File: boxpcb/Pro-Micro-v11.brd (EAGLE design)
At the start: 40 x 74 mm, 30 parts

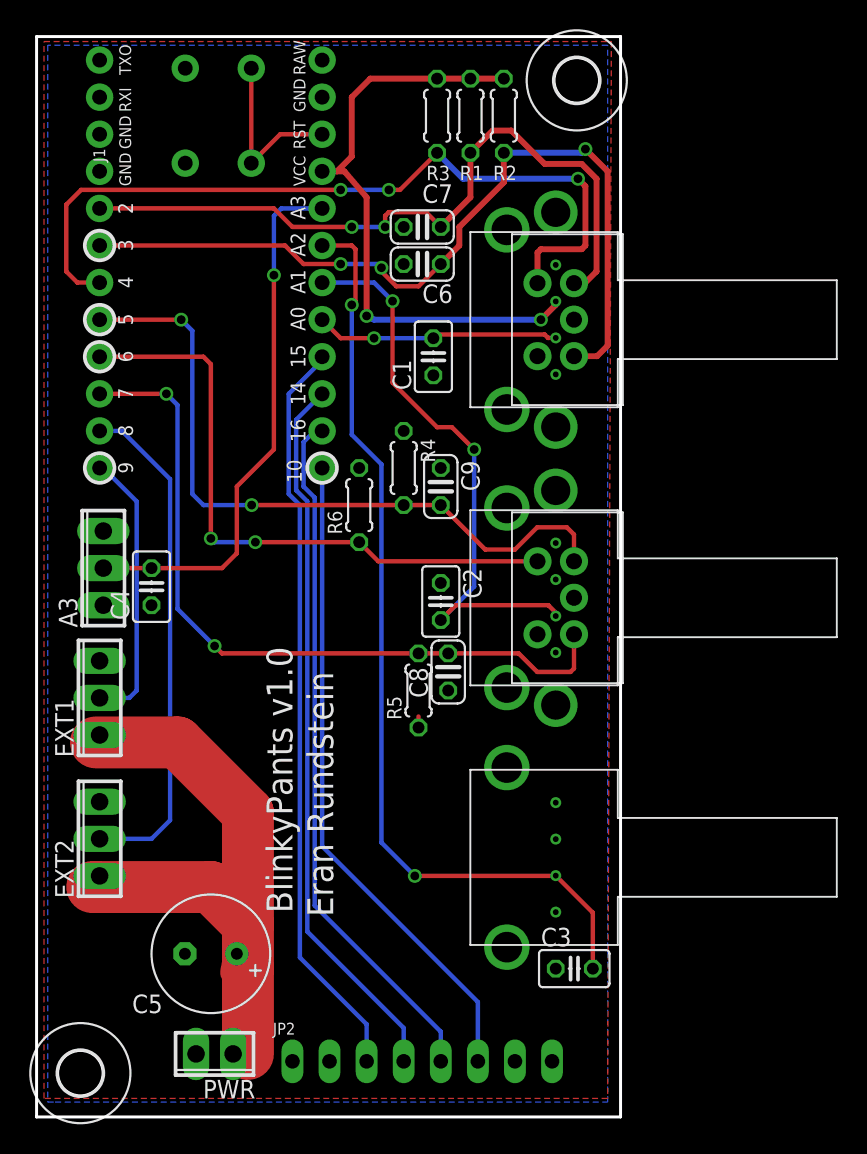
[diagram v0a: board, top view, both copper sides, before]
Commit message: pcb simplification - remove dual rot/pot
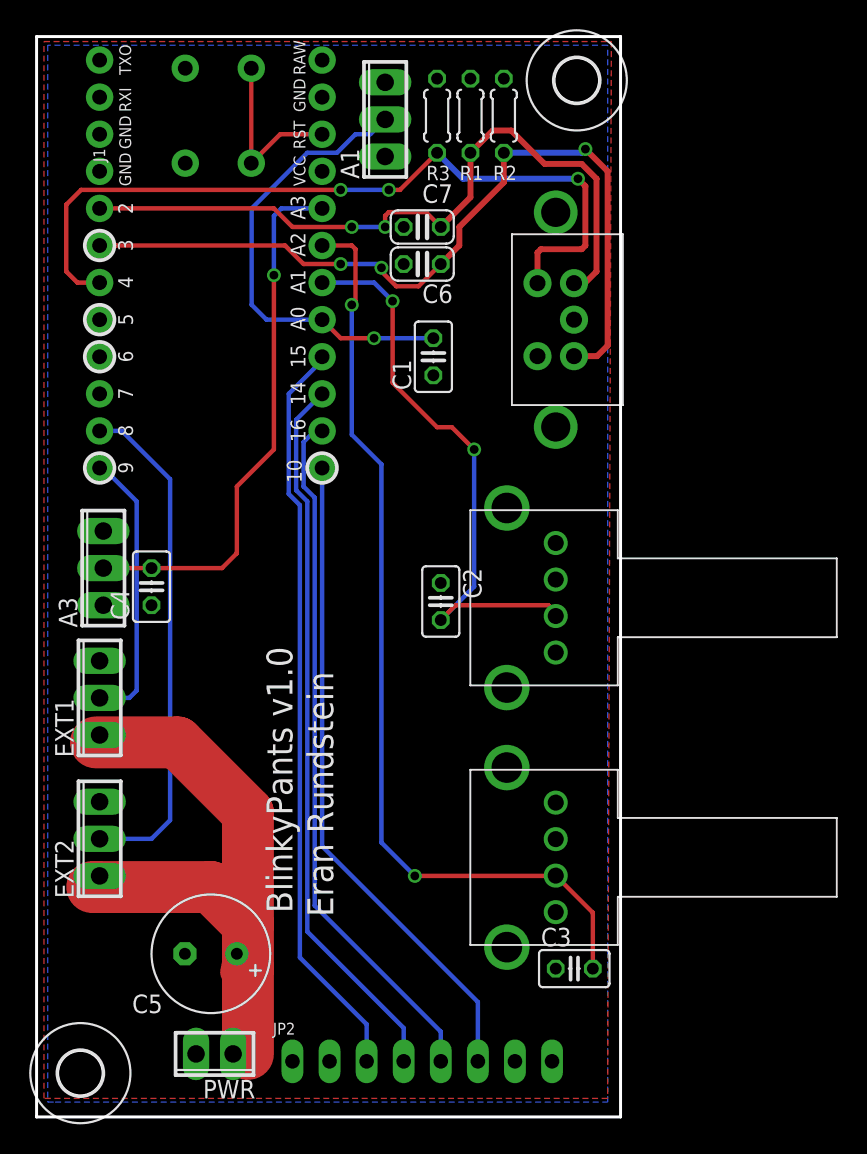
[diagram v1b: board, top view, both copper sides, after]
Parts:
- removed C8, C9: 0.1uF, rcl:C025-024X044
- removed R4, R5, R6: 47K, rcl:0204/5
- removed U$1: P110KV1-1F15BRP110KV1-1F15BR, keves:P110KV1-1F15BR
- removed U$5: EN11-VSM1AF20, rotary-encoder:EN11-VS*
- added A1: (no value), con-phoenix-254:3POL254
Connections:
- net A0: now also A1.2; no longer U$1.P$2
- net D5: no longer C9.2, R4.2, U$5.B
- net D6: no longer R6.1, U$5.E
- net D7: no longer C8.2, R5.2, U$5.A
- net GND: now also A1.3; no longer C8.1, C9.1, U$1.P$1, U$5.C, U$5.D
- net VCC: now also A1.1; no longer R4.1, R5.1, R6.2, U$1.P$3
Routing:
- net D7: track 51.0 -> 0.00 mm, vias 2 -> 0
- net D5: track 48.2 -> 0.00 mm, vias 2 -> 0
- net VCC: track 90.4 -> 47.5 mm, vias 2 -> 0
- net D6: track 42.8 -> 0.00 mm, vias 2 -> 0
- net A0: track 16.7 -> 31.7 mm

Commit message: wip
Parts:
- removed A1: (no value), con-phoenix-254:3POL254
- added A2: (no value), con-phoenix-254:3POL254
- moved R2 22.7 mm to (28.2, 46.2), turned to 90 degrees
- moved C1 15.5 mm to (28.2, 67.6), turned to 180 degrees
- moved C6 11.7 mm to (30.5, 47.5), turned to 90 degrees
- moved R3 11.5 mm to (28.2, 57.1), turned to 180 degrees
- moved R1 6.71 mm to (26.9, 62.5)
- moved C7 3.06 mm to (29.5, 61.2), turned to 270 degrees
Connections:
- net A0: now also C3.2, U$4.P$2; no longer A1.2, C1.2
- net A2: now also A2.2, C1.2; no longer C3.2, U$4.P$2
- net GND: now also A2.3; no longer A1.3
- net VCC: now also A2.1; no longer A1.1
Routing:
- net A2: track 64.3 -> 15.7 mm, vias 2 -> 0
- net A0: track 31.7 -> 60.6 mm, vias 1 -> 0
- net D4: track 54.8 -> 33.1 mm, vias 3 -> 2
- net D3: track 57.1 -> 40.0 mm, vias 3 -> 2
- net D2: track 50.0 -> 36.0 mm, vias 2 -> 1
- net A1: track 40.2 -> 36.8 mm, vias 2 -> 0
- net A3: track 37.2 -> 38.0 mm, vias 1 -> 0
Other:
- board text added: "+"

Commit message: board stuff
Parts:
- moved C1 3.31 mm to (31.0, 65.8)
- moved C3 2.50 mm to (35.8, 7.87)
- moved A2 1.80 mm to (26.7, 69.3)
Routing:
- net A2: track 15.7 -> 18.9 mm, vias 0 -> 1
- net A1: track 36.8 -> 37.6 mm
- net A0: track 60.6 -> 61.2 mm
- net D4: track 33.1 -> 32.7 mm, vias 2 -> 1
- net D3: track 40.0 -> 39.9 mm, vias 2 -> 3
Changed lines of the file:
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@@
 </class>
 </classes>
-<designrules name="oshpark_2layer">
+<designrules name="oshpark_2layer *">
 <description language="de">&lt;b&gt;EAGLE Design Rules&lt;/b&gt;
 &lt;p&gt;
@@
 <param name="rvMicroViaOuter" value="0.25"/>
 <param name="rvMicroViaInner" value="0.25"/>
-<param name="rlMinPadTop" value="7mil"/>
+<param name="rlMinPadTop" value="12mil"/>
 <param name="rlMaxPadTop" value="20mil"/>
 <param name="rlMinPadInner" value="7mil"/>
@@
 <param name="mlMinCreamFrame" value="0mil"/>
 <param name="mlMaxCreamFrame" value="0mil"/>
-<param name="mlViaStopLimit" value="0mil"/>
+<param name="mlViaStopLimit" value="20mil"/>
 <param name="srRoundness" value="0"/>
 <param name="srMinRoundness" value="0mil"/>
@@
 <element name="U$3" library="rotary-encoder" package="EN11-VS*" value="EN11-VSM1AF20" x="35.56" y="54.61" rot="R90"/>
 <element name="U$4" library="keves" package="P110KV1-1F15BR" value="P110KV1-1F15BRP110KV1-1F15BR" x="35.56" y="17.78" rot="R90"/>
-<element name="C1" library="rcl" package="C025-025X050" value="0.1uF" x="28.194" y="67.564" rot="R180"/>
+<element name="C1" library="rcl" package="C025-025X050" value="0.1uF" x="30.988" y="65.786" rot="R180"/>
 <element name="C2" library="rcl" package="C025-025X050" value="0.1uF" x="27.686" y="35.306" rot="R270"/>
-<element name="C3" library="rcl" package="C025-025X050" value="0.1uF" x="36.83" y="10.16"/>
+<element name="C3" library="rcl" package="C025-025X050" value="0.1uF" x="35.814" y="7.874"/>
 <element name="C4" library="rcl" package="C025-025X050" value="0.1uF" x="7.874" y="36.322" rot="R90"/>
 <element name="R1" library="rcl" package="0204/5" value="47K" x="26.924" y="62.484" smashed="yes" rot="R270">
@@
 <element name="H1" library="holes" package="3,0" value="MOUNT-HOLE3.0" x="3" y="3"/>
 <element name="H2" library="holes" package="3,0" value="MOUNT-HOLE3.0" x="37" y="71"/>
-<element name="A2" library="con-phoenix-254" package="3POL254" value="" x="26.924" y="71.12" rot="R180">
-<attribute name="OC_NEWARK" value="unknown" x="26.924" y="71.12" size="1.778" layer="27" font="vector" rot="R180" display="off"/>
-<attribute name="MPN" value="" x="26.924" y="71.12" size="1.778" layer="27" font="vector" rot="R180" display="off"/>
-<attribute name="MF" value="" x="26.924" y="71.12" size="1.778" layer="27" font="vector" rot="R180" display="off"/>
-<attribute name="OC_FARNELL" value="unknown" x="26.924" y="71.12" size="1.778" layer="27" font="vector" rot="R180" display="off"/>
+<element name="A2" library="con-phoenix-254" package="3POL254" value="" x="26.67" y="69.342" rot="R180">
+<attribute name="OC_NEWARK" value="unknown" x="26.67" y="69.342" size="1.778" layer="27" font="vector" rot="R180" display="off"/>
+<attribute name="MPN" value="" x="26.67" y="69.342" size="1.778" layer="27" font="vector" rot="R180" display="off"/>
+<attribute name="MF" value="" x="26.67" y="69.342" size="1.778" layer="27" font="vector" rot="R180" display="off"/>
+<attribute name="OC_FARNELL" value="unknown" x="26.67" y="69.342" size="1.778" layer="27" font="vector" rot="R180" display="off"/>
 </element>
 </elements>
@@
 <contactref element="JP2" pad="7"/>
 <contactref element="JP2" pad="8"/>
-<polygon width="0.762" layer="16">
+<polygon width="0.762" layer="16" isolate="0.3048">
 <vertex x="1.27" y="1.016"/>
 <vertex x="39.116" y="1.016"/>
@@
 <wire x1="4.318" y1="16.002" x2="4.064" y2="15.748" width="1.778" layer="1"/>
 <contactref element="A3" pad="1"/>
-<polygon width="0.3048" layer="1">
+<polygon width="0.3048" layer="1" isolate="0.3048">
 <vertex x="0.508" y="73.66"/>
 <vertex x="39.37" y="73.66"/>
@@
 <wire x1="19.558" y1="59.69" x2="21.336" y2="59.69" width="0.3048" layer="1"/>
 <wire x1="21.336" y1="59.69" x2="22.606" y2="60.96" width="0.3048" layer="1"/>
-<wire x1="22.606" y1="60.96" x2="22.606" y2="63.754" width="0.3048" layer="1"/>
-<wire x1="22.606" y1="63.754" x2="26.924" y2="67.564" width="0.3048" layer="1"/>
-<wire x1="26.924" y1="71.12" x2="26.924" y2="67.564" width="0.3048" layer="1"/>
+<wire x1="22.606" y1="60.96" x2="22.606" y2="64.262" width="0.3048" layer="1"/>
+<wire x1="29.718" y1="65.786" x2="28.956" y2="65.786" width="0.3048" layer="1"/>
+<wire x1="28.956" y1="65.786" x2="26.67" y2="68.072" width="0.3048" layer="1"/>
+<wire x1="26.67" y1="68.072" x2="26.67" y2="69.342" width="0.3048" layer="1"/>
+<wire x1="22.606" y1="64.262" x2="23.368" y2="65.024" width="0.3048" layer="1"/>
+<via x="23.368" y="65.024" extent="1-16" drill="0.6"/>
+<wire x1="23.368" y1="65.024" x2="26.67" y2="68.326" width="0.3048" layer="16"/>
+<wire x1="26.67" y1="68.326" x2="26.67" y2="69.342" width="0.3048" layer="16"/>
 </signal>
 <signal name="A1">
@@
 <contactref element="U$2" pad="P$2"/>
 <contactref element="C2" pad="2"/>
-<wire x1="19.558" y1="57.15" x2="20.828" y2="57.15" width="0.3048" layer="1"/>
-<wire x1="20.828" y1="57.15" x2="23.114" y2="54.864" width="0.3048" layer="1"/>
-<wire x1="23.114" y1="54.864" x2="23.114" y2="35.814" width="0.3048" layer="1"/>
-<wire x1="23.114" y1="35.814" x2="24.892" y2="34.036" width="0.3048" layer="1"/>
-<wire x1="27.686" y1="34.036" x2="24.892" y2="34.036" width="0.3048" layer="1"/>
 <wire x1="27.686" y1="34.036" x2="35.286" y2="34.036" width="0.3048" layer="1"/>
 <wire x1="35.286" y1="34.036" x2="35.56" y2="34.31" width="0.3048" layer="1"/>
+<wire x1="19.558" y1="57.15" x2="20.066" y2="57.15" width="0.3048" layer="16"/>
+<wire x1="20.066" y1="57.15" x2="22.352" y2="54.864" width="0.3048" layer="16"/>
+<wire x1="22.352" y1="54.864" x2="22.352" y2="34.544" width="0.3048" layer="16"/>
+<wire x1="22.352" y1="34.544" x2="22.86" y2="34.036" width="0.3048" layer="16"/>
+<wire x1="22.86" y1="34.036" x2="27.686" y2="34.036" width="0.3048" layer="16"/>
 </signal>
 <signal name="A0">
@@
 <contactref element="U$4" pad="P$2"/>
 <contactref element="C3" pad="2"/>
-<wire x1="38.1" y1="10.16" x2="38.1" y2="13.99" width="0.3048" layer="1"/>
-<wire x1="38.1" y1="13.99" x2="35.56" y2="16.53" width="0.3048" layer="1"/>
-<wire x1="19.558" y1="54.61" x2="21.336" y2="54.61" width="0.3048" layer="1"/>
-<wire x1="21.336" y1="54.61" x2="22.098" y2="53.848" width="0.3048" layer="1"/>
-<wire x1="22.098" y1="53.848" x2="22.098" y2="17.272" width="0.3048" layer="1"/>
-<wire x1="22.098" y1="17.272" x2="22.86" y2="16.51" width="0.3048" layer="1"/>
-<wire x1="22.86" y1="16.51" x2="35.54" y2="16.51" width="0.3048" layer="1"/>
-<wire x1="35.54" y1="16.51" x2="35.56" y2="16.53" width="0.3048" layer="1"/>
+<wire x1="19.558" y1="54.61" x2="20.32" y2="54.61" width="0.3048" layer="16"/>
+<wire x1="20.32" y1="54.61" x2="21.336" y2="53.594" width="0.3048" layer="16"/>
+<wire x1="21.336" y1="53.594" x2="21.336" y2="19.304" width="0.3048" layer="16"/>
+<wire x1="21.336" y1="19.304" x2="24.13" y2="16.51" width="0.3048" layer="16"/>
+<wire x1="24.13" y1="16.51" x2="35.54" y2="16.51" width="0.3048" layer="16"/>
+<wire x1="35.54" y1="16.51" x2="35.56" y2="16.53" width="0.3048" layer="16"/>
+<wire x1="37.084" y1="7.874" x2="37.084" y2="15.006" width="0.3048" layer="1"/>
+<wire x1="37.084" y1="15.006" x2="35.56" y2="16.53" width="0.3048" layer="1"/>
 </signal>
 <signal name="D2">
@@
 <contactref element="R2" pad="2"/>
 <contactref element="C6" pad="2"/>
-<wire x1="28.194" y1="48.768" x2="28.448" y2="48.768" width="0.3048" layer="1"/>
-<wire x1="28.448" y1="48.768" x2="30.48" y2="48.768" width="0.3048" layer="1"/>
+<wire x1="28.194" y1="48.768" x2="30.48" y2="48.768" width="0.3048" layer="1"/>
 <wire x1="30.48" y1="48.768" x2="33.02" y2="48.768" width="0.3048" layer="1"/>
 <wire x1="33.02" y1="48.768" x2="34.29" y2="50.038" width="0.3048" layer="1"/>
@@
 <wire x1="21.082" y1="58.42" x2="16.51" y2="58.42" width="0.254" layer="1"/>
 <wire x1="21.082" y1="58.166" x2="21.082" y2="58.42" width="0.254" layer="1"/>
-<wire x1="28.448" y1="50.8" x2="21.082" y2="58.166" width="0.254" layer="1"/>
-<wire x1="28.448" y1="48.768" x2="28.448" y2="50.8" width="0.254" layer="1"/>
 <via x="13.716" y="59.69" extent="1-16" drill="0.3302"/>
 <via x="15.24" y="59.69" extent="1-16" drill="0.3302"/>
+<wire x1="21.082" y1="58.166" x2="25.654" y2="53.594" width="0.3048" layer="1"/>
+<via x="25.654" y="53.594" extent="1-16" drill="0.6"/>
+<wire x1="25.654" y1="53.594" x2="28.194" y2="51.054" width="0.3048" layer="16"/>
+<wire x1="28.194" y1="51.054" x2="28.194" y2="48.768" width="0.3048" layer="16"/>
 </signal>
 <signal name="D4">
@@
 <contactref element="U$3" pad="E"/>
 <contactref element="R3" pad="1"/>
-<wire x1="34.31" y1="57.11" x2="30.774" y2="57.11" width="0.3048" layer="1"/>
 <wire x1="30.774" y1="57.11" x2="30.734" y2="57.15" width="0.3048" layer="1"/>
 <wire x1="13.716" y1="57.15" x2="4.318" y2="57.15" width="0.254" layer="1"/>
 <wire x1="14.986" y1="58.42" x2="13.716" y2="57.15" width="0.254" layer="16"/>
 <wire x1="21.844" y1="58.42" x2="14.986" y2="58.42" width="0.254" layer="16"/>
-<wire x1="24.638" y1="55.626" x2="21.844" y2="58.42" width="0.254" layer="1"/>
-<wire x1="30.48" y1="55.626" x2="24.638" y2="55.626" width="0.254" layer="1"/>
-<wire x1="30.48" y1="56.896" x2="30.48" y2="55.626" width="0.254" layer="1"/>
 <wire x1="30.734" y1="57.15" x2="30.48" y2="56.896" width="0.254" layer="1"/>
 <via x="13.716" y="57.15" extent="1-16" drill="0.3302"/>
-<via x="21.844" y="58.42" extent="1-16" drill="0.3302"/>
+<wire x1="34.31" y1="57.11" x2="30.774" y2="57.11" width="0.3048" layer="16"/>
+<wire x1="30.774" y1="57.11" x2="30.734" y2="57.15" width="0.3048" layer="16"/>
+<wire x1="21.844" y1="58.42" x2="24.638" y2="55.626" width="0.3048" layer="16"/>
+<wire x1="24.638" y1="55.626" x2="29.21" y2="55.626" width="0.3048" layer="16"/>
+<wire x1="29.21" y1="55.626" x2="30.734" y2="57.15" width="0.3048" layer="16"/>
 </signal>
 <signal name="D5">
